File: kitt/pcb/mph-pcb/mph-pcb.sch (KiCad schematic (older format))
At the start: 15 parts, among them U1 TLC5940NT, U2 TLC5940NT, U3 TLC5940NT, U4 TLC5940NT, U5 TLC5940NT, U6 TLC5940NT, U7 TLC5940NT

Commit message: first four 7-segment displays
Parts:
- added DISP1, DISP2, DISP3, DISP4: LDS-A816RI, Display_7Segment:7SegmentLED_LDSA816RI_LDSA816RI, symbol Display_Character:LDS-A816RI
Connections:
- net labels added: DISP1_A, DISP1_B, DISP1_C, DISP1_D, DISP1_E, DISP1_F, DISP1_G, DISP1_RDP, DISP2_A, DISP2_B, DISP2_C, DISP2_D, DISP2_E, DISP2_F, DISP2_G, DISP2_RDP, DISP3_A, DISP3_B, DISP3_C, DISP3_D, DISP3_E, DISP3_F, DISP3_G, DISP3_RDP, DISP4_A, DISP4_B, DISP4_C, DISP4_D, DISP4_E, DISP4_F, DISP4_G, DISP4_RDP
- wire segments 65 -> 117
- no-connect marks 14 -> 18

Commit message: store all libraries in project
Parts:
- DISP1, DISP2, DISP3, DISP4: symbol Display_Character:LDS-A816RI -> KITT-Symbols:LDS-A816RI
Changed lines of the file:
@@
 NoConn ~ 3450 14600
 $Comp
-L Display_Character:LDS-A816RI DISP1
+L KITT-Symbols:LDS-A816RI DISP1
 U 1 1 61139383
 P 3500 9100
@@
 NoConn ~ 4000 9400
 $Comp
-L Display_Character:LDS-A816RI DISP2
+L KITT-Symbols:LDS-A816RI DISP2
 U 1 1 6114598A
 P 5000 9100
@@
 NoConn ~ 5500 9400
 $Comp
-L Display_Character:LDS-A816RI DISP3
+L KITT-Symbols:LDS-A816RI DISP3
 U 1 1 61149F6E
 P 6500 9100
@@
 NoConn ~ 7000 9400
 $Comp
-L Display_Character:LDS-A816RI DISP4
+L KITT-Symbols:LDS-A816RI DISP4
 U 1 1 6114DA45
 P 8000 9100

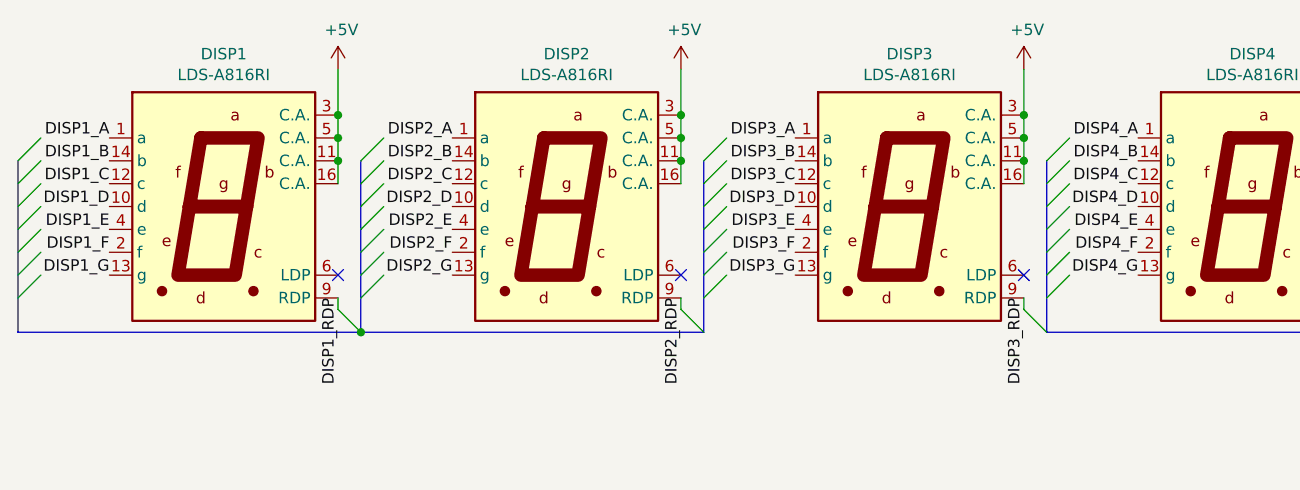
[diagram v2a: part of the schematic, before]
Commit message: wire up a-f on displays
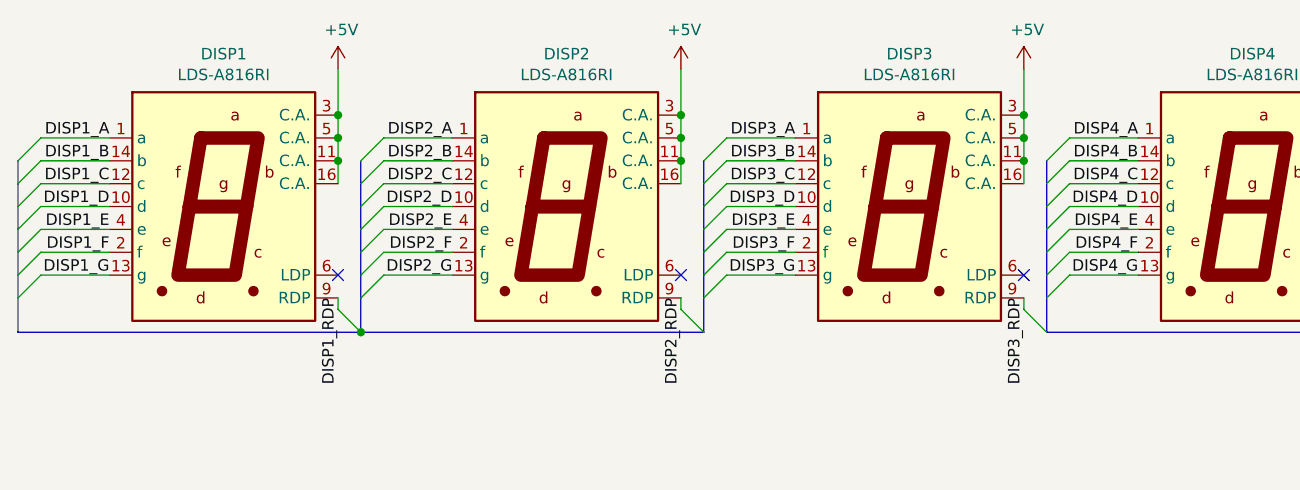
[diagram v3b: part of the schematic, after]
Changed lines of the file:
@@
 Wire Wire Line
 	7400 10500 7400 10950
+Wire Wire Line
+	2700 8800 3000 8800
+Wire Wire Line
+	2700 8900 3000 8900
+Wire Wire Line
+	2700 9000 3000 9000
+Wire Wire Line
+	3000 9100 2700 9100
+Wire Wire Line
+	3000 9200 2700 9200
+Wire Wire Line
+	3000 9300 2700 9300
+Wire Wire Line
+	3000 9400 2700 9400
+Wire Wire Line
+	4500 9400 4200 9400
+Wire Wire Line
+	4500 9300 4200 9300
+Wire Wire Line
+	4500 9200 4200 9200
+Wire Wire Line
+	4500 9100 4200 9100
+Wire Wire Line
+	4500 9000 4200 9000
+Wire Wire Line
+	4500 8900 4200 8900
+Wire Wire Line
+	4500 8800 4200 8800
+Wire Wire Line
+	6000 9400 5700 9400
+Wire Wire Line
+	6000 9300 5700 9300
+Wire Wire Line
+	6000 9200 5700 9200
+Wire Wire Line
+	6000 9100 5700 9100
+Wire Wire Line
+	6000 9000 5700 9000
+Wire Wire Line
+	6000 8900 5700 8900
+Wire Wire Line
+	6000 8800 5700 8800
+Wire Wire Line
+	7500 9400 7200 9400
+Wire Wire Line
+	7500 9300 7200 9300
+Wire Wire Line
+	7500 9200 7200 9200
+Wire Wire Line
+	7500 9100 7200 9100
+Wire Wire Line
+	7500 9000 7200 9000
+Wire Wire Line
+	7500 8900 7200 8900
+Wire Wire Line
+	7500 8800 7200 8800
 Wire Bus Line
 	2900 13250 2900 14700

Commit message: fixed footpads
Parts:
- DISP1, DISP2, DISP3, DISP4: footprint Display_7Segment:7SegmentLED_LDSA816RI_LDSA816RI -> KITT-Footpads:LDS-A816RI
- TTGO1: footprint TTGO-tdisplay:TTGO_ESP32_TDisplay_v1.1 -> KITT-Footpads:TTGO_ESP32_TDisplay_v1.1
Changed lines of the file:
@@
 F 0 "TTGO1" H 4000 16587 60  0000 C CNN
 F 1 "TTGO_ESP32_TDISPLAY_V1.1" H 4000 16481 60  0000 C CNN
-F 2 "TTGO-tdisplay:TTGO_ESP32_TDisplay_v1.1" H 3650 15150 60  0001 C CNN
+F 2 "KITT-Footpads:TTGO_ESP32_TDisplay_v1.1" H 3650 15150 60  0001 C CNN
 F 3 "" H 3650 15150 60  0001 C CNN
 	1    3650 15150
@@
 F 0 "DISP1" H 3500 9767 50  0000 C CNN
 F 1 "LDS-A816RI" H 3500 9676 50  0000 C CNN
-F 2 "Display_7Segment:7SegmentLED_LDSA816RI_LDSA816RI" H 3500 8500 50  0001 C CNN
-F 3 "https://datasheet.octopart.com/LTS-6960HR-Lite-On-datasheet-11803242.pdf" H 4450 9050 50  0001 C CNN
+F 2 "KITT-Footpads:LDS-A816RI" H 3500 8500 50  0001 C CNN
+F 3 "https://www.lumex.com/datasheet/LDS-A816RI" H 4450 9050 50  0001 C CNN
 	1    3500 9100
 	1    0    0    -1
@@
 	4000 8900 4000 8800
 $Comp
-L power:+5V #PWR?
+L power:+5V #PWR0128
 U 1 1 6113BF63
 P 4000 8500
-F 0 "#PWR?" H 4000 8350 50  0001 C CNN
+F 0 "#PWR0128" H 4000 8350 50  0001 C CNN
 F 1 "+5V" H 4015 8673 50  0000 C CNN
 F 2 "" H 4000 8500 50  0001 C CNN
@@
 F 0 "DISP2" H 5000 9767 50  0000 C CNN
 F 1 "LDS-A816RI" H 5000 9676 50  0000 C CNN
-F 2 "Display_7Segment:7SegmentLED_LDSA816RI_LDSA816RI" H 5000 8500 50  0001 C CNN
-F 3 "https://datasheet.octopart.com/LTS-6960HR-Lite-On-datasheet-11803242.pdf" H 5950 9050 50  0001 C CNN
+F 2 "KITT-Footpads:LDS-A816RI" H 5000 8500 50  0001 C CNN
+F 3 "https://www.lumex.com/datasheet/LDS-A816RI" H 5950 9050 50  0001 C CNN
 	1    5000 9100
 	1    0    0    -1
@@
 	5500 8900 5500 8800
 $Comp
-L power:+5V #PWR?
+L power:+5V #PWR0129
 U 1 1 61145997
 P 5500 8500
-F 0 "#PWR?" H 5500 8350 50  0001 C CNN
+F 0 "#PWR0129" H 5500 8350 50  0001 C CNN
 F 1 "+5V" H 5515 8673 50  0000 C CNN
 F 2 "" H 5500 8500 50  0001 C CNN
@@
 F 0 "DISP3" H 6500 9767 50  0000 C CNN
 F 1 "LDS-A816RI" H 6500 9676 50  0000 C CNN
-F 2 "Display_7Segment:7SegmentLED_LDSA816RI_LDSA816RI" H 6500 8500 50  0001 C CNN
-F 3 "https://datasheet.octopart.com/LTS-6960HR-Lite-On-datasheet-11803242.pdf" H 7450 9050 50  0001 C CNN
+F 2 "KITT-Footpads:LDS-A816RI" H 6500 8500 50  0001 C CNN
+F 3 "https://www.lumex.com/datasheet/LDS-A816RI" H 7450 9050 50  0001 C CNN
 	1    6500 9100
 	1    0    0    -1
@@
 	7000 8900 7000 8800
 $Comp
-L power:+5V #PWR?
+L power:+5V #PWR0130
 U 1 1 61149F7B
 P 7000 8500
-F 0 "#PWR?" H 7000 8350 50  0001 C CNN
+F 0 "#PWR0130" H 7000 8350 50  0001 C CNN
 F 1 "+5V" H 7015 8673 50  0000 C CNN
 F 2 "" H 7000 8500 50  0001 C CNN
@@
 F 0 "DISP4" H 8000 9767 50  0000 C CNN
 F 1 "LDS-A816RI" H 8000 9676 50  0000 C CNN
-F 2 "Display_7Segment:7SegmentLED_LDSA816RI_LDSA816RI" H 8000 8500 50  0001 C CNN
-F 3 "https://datasheet.octopart.com/LTS-6960HR-Lite-On-datasheet-11803242.pdf" H 8950 9050 50  0001 C CNN
+F 2 "KITT-Footpads:LDS-A816RI" H 8000 8500 50  0001 C CNN
+F 3 "https://www.lumex.com/datasheet/LDS-A816RI" H 8950 9050 50  0001 C CNN
 	1    8000 9100
 	1    0    0    -1
@@
 	8500 8900 8500 8800
 $Comp
-L power:+5V #PWR?
+L power:+5V #PWR0131
 U 1 1 6114DA52
 P 8500 8500
-F 0 "#PWR?" H 8500 8350 50  0001 C CNN
+F 0 "#PWR0131" H 8500 8350 50  0001 C CNN
 F 1 "+5V" H 8515 8673 50  0000 C CNN
 F 2 "" H 8500 8500 50  0001 C CNN

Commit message: add coupling capacitors
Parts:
- added C1: 100nF, symbol Device:C
- added C2: 1uF, symbol Device:C
- added C3, C4, C5, C6, C7, C8, C9: 100nF, Capacitor_THT:C_Rect_L7.0mm_W3.5mm_P5.00mm, symbol Device:C
- R1, R2, R3, R4, R5, R7: footprint (none) -> Resistor_THT:R_Axial_DIN0207_L6.3mm_D2.5mm_P10.16mm_Horizontal
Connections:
- net +5V: now also C1.1, C2.1, C3.1, C4.1, C5.1, C6.1, C7.1, C8.1, C9.1
- net GND: now also C1.2, C2.2, C3.2, C4.2, C5.2, C6.2, C7.2, C8.2, C9.2

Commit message: fixed missing footpads
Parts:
- C1, C2: footprint (none) -> Capacitor_THT:C_Rect_L7.0mm_W3.5mm_P5.00mm
- R6: footprint (none) -> Resistor_THT:R_Axial_DIN0207_L6.3mm_D2.5mm_P10.16mm_Horizontal
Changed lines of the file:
@@
 F 0 "R6" H 16470 12796 50  0000 L CNN
 F 1 "2.2K" H 16470 12705 50  0000 L CNN
-F 2 "" V 16330 12750 50  0001 C CNN
+F 2 "Resistor_THT:R_Axial_DIN0207_L6.3mm_D2.5mm_P10.16mm_Horizontal" V 16330 12750 50  0001 C CNN
 F 3 "~" H 16400 12750 50  0001 C CNN
 	1    16400 12750
@@
 $EndComp
 $Comp
-L power:GND #PWR?
+L power:GND #PWR0132
 U 1 1 61134539
 P 2800 11950
-F 0 "#PWR?" H 2800 11700 50  0001 C CNN
+F 0 "#PWR0132" H 2800 11700 50  0001 C CNN
 F 1 "GND" H 2805 11777 50  0000 C CNN
 F 2 "" H 2800 11950 50  0001 C CNN
@@
 $EndComp
 $Comp
-L power:GND #PWR?
+L power:GND #PWR0133
 U 1 1 6115CD6C
 P 5400 11950
-F 0 "#PWR?" H 5400 11700 50  0001 C CNN
+F 0 "#PWR0133" H 5400 11700 50  0001 C CNN
 F 1 "GND" H 5405 11777 50  0000 C CNN
 F 2 "" H 5400 11950 50  0001 C CNN
@@
 $EndComp
 $Comp
-L power:GND #PWR?
+L power:GND #PWR0134
 U 1 1 6116FAF1
 P 8000 11950
-F 0 "#PWR?" H 8000 11700 50  0001 C CNN
+F 0 "#PWR0134" H 8000 11700 50  0001 C CNN
 F 1 "GND" H 8005 11777 50  0000 C CNN
 F 2 "" H 8000 11950 50  0001 C CNN
@@
 $EndComp
 $Comp
-L power:GND #PWR?
+L power:GND #PWR0135
 U 1 1 61182311
 P 10600 11950
-F 0 "#PWR?" H 10600 11700 50  0001 C CNN
+F 0 "#PWR0135" H 10600 11700 50  0001 C CNN
 F 1 "GND" H 10605 11777 50  0000 C CNN
 F 2 "" H 10600 11950 50  0001 C CNN
@@
 $EndComp
 $Comp
-L power:GND #PWR?
+L power:GND #PWR0136
 U 1 1 611950CA
 P 13200 11950
-F 0 "#PWR?" H 13200 11700 50  0001 C CNN
+F 0 "#PWR0136" H 13200 11700 50  0001 C CNN
 F 1 "GND" H 13205 11777 50  0000 C CNN
 F 2 "" H 13200 11950 50  0001 C CNN
@@
 $EndComp
 $Comp
-L power:GND #PWR?
+L power:GND #PWR0137
 U 1 1 611A7D7F
 P 15800 11950
-F 0 "#PWR?" H 15800 11700 50  0001 C CNN
+F 0 "#PWR0137" H 15800 11700 50  0001 C CNN
 F 1 "GND" H 15805 11777 50  0000 C CNN
 F 2 "" H 15800 11950 50  0001 C CNN
@@
 $EndComp
 $Comp
-L power:GND #PWR?
+L power:GND #PWR0138
 U 1 1 611BAA79
 P 18400 11950
-F 0 "#PWR?" H 18400 11700 50  0001 C CNN
+F 0 "#PWR0138" H 18400 11700 50  0001 C CNN
 F 1 "GND" H 18405 11777 50  0000 C CNN
 F 2 "" H 18400 11950 50  0001 C CNN
@@
 F 0 "C1" H 4665 15296 50  0000 L CNN
 F 1 "100nF" H 4665 15205 50  0000 L CNN
-F 2 "" H 4588 15100 50  0001 C CNN
+F 2 "Capacitor_THT:C_Rect_L7.0mm_W3.5mm_P5.00mm" H 4588 15100 50  0001 C CNN
 F 3 "~" H 4550 15250 50  0001 C CNN
 	1    4550 15250
@@
 Connection ~ 4550 15100
 $Comp
-L power:GND #PWR?
+L power:GND #PWR0139
 U 1 1 611E2E2D
 P 4550 15400
-F 0 "#PWR?" H 4550 15150 50  0001 C CNN
+F 0 "#PWR0139" H 4550 15150 50  0001 C CNN
 F 1 "GND" H 4555 15227 50  0000 C CNN
 F 2 "" H 4550 15400 50  0001 C CNN
@@
 F 0 "C2" H 5165 15296 50  0000 L CNN
 F 1 "1uF" H 5165 15205 50  0000 L CNN
-F 2 "" H 5088 15100 50  0001 C CNN
+F 2 "Capacitor_THT:C_Rect_L7.0mm_W3.5mm_P5.00mm" H 5088 15100 50  0001 C CNN
 F 3 "~" H 5050 15250 50  0001 C CNN
 	1    5050 15250
@@
 Connection ~ 5050 15100
 $Comp
-L power:GND #PWR?
+L power:GND #PWR0140
 U 1 1 611191EF
 P 5050 15400
-F 0 "#PWR?" H 5050 15150 50  0001 C CNN
+F 0 "#PWR0140" H 5050 15150 50  0001 C CNN
 F 1 "GND" H 5055 15227 50  0000 C CNN
 F 2 "" H 5050 15400 50  0001 C CNN

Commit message: finished wiring
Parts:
- added D25, D26, D27, HT1, HT10, HT11, HT12, HT13, HT14, HT15, HT16, HT2, HT3, HT4, HT5, HT6, HT7, HT8, HT9, HY1, HY2, HY3, MY1, MY2, MY3, UG1, UG10, UG11, UG12, UG13, UG14, UG15, UG16, UG17, UG18, UG19, UG2, UG20, UG3, UG4, UG5, UG6, UG7, UG8, UG9, UGY1, UGY2, UGY3: LED, symbol Device:LED
- added GUID1, GUID2, SYST1, SYST2: DF3GD, symbol KITT-Symbols:DF3GD
- added J1, J2: Screw_Terminal_01x02, symbol Connector:Screw_Terminal_01x02
- added LVL1: LVL_5V_3V3, symbol KITT-Symbols:LVL_5V_3V3
- added PWR1: OKI-78SR-3.3_1.5-W36H-C, Converter_DCDC:Converter_DCDC_muRata_OKI-78SR_Horizontal, symbol Converter_DCDC:OKI-78SR-3.3_1.5-W36H-C
- added R10, R11, R12, R13, R14, R15, R16, R17, R18, R19, R8, R9: 120R, Resistor_THT:R_Axial_DIN0207_L6.3mm_D2.5mm_P10.16mm_Horizontal, symbol Device:R
- added UT_DISP1, UT_DISP2, UT_DISP3: LDS-A816RI, KITT-Footpads:LDS-A816RI, symbol KITT-Symbols:LDS-A816RI
- renumbered DISP2 to HLT_DISP2, DISP1 to MASH_DISP1, DISP3 to MASH_DISP3, DISP4 to MASH_DISP4
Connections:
- net +5V: now also D25.2 (A), D26.2 (A), D27.2 (A), HT1.2 (A), HT10.2 (A), HT11.2 (A), HT12.2 (A), HT13.2 (A), HT14.2 (A), HT15.2 (A), HT16.2 (A), HT2.2 (A), HT3.2 (A), HT4.2 (A), HT5.2 (A), HT6.2 (A), HT7.2 (A), HT8.2 (A), HT9.2 (A), HY1.2 (A), HY2.2 (A), HY3.2 (A), LVL1.1 (5V), MY1.2 (A), MY2.2 (A), MY3.2 (A), PWR1.3 (OUT), R10.1, R11.1, R12.1, R13.1, R14.1, R15.1, R16.1, R17.1, R18.1, R19.1, R8.1, R9.1, UG1.2 (A), UG10.2 (A), UG11.2 (A), UG12.2 (A), UG13.2 (A), UG14.2 (A), UG15.2 (A), UG16.2 (A), UG17.2 (A), UG18.2 (A), UG19.2 (A), UG2.2 (A), UG20.2 (A), UG3.2 (A), UG4.2 (A), UG5.2 (A), UG6.2 (A), UG7.2 (A), UG8.2 (A), UG9.2 (A), UGY1.2 (A), UGY2.2 (A), UGY3.2 (A), UT_DISP1.11 (C.A.), UT_DISP1.16 (C.A.), UT_DISP1.3 (C.A.), UT_DISP1.5 (C.A.), UT_DISP2.11 (C.A.), UT_DISP2.16 (C.A.), UT_DISP2.3 (C.A.), UT_DISP2.5 (C.A.), UT_DISP3.11 (C.A.), UT_DISP3.16 (C.A.), UT_DISP3.3 (C.A.), UT_DISP3.5 (C.A.)
- net GND: now also GUID1.2 (D3C), GUID1.4 (D2C), GUID1.6 (D1C), GUID2.2 (D3C), GUID2.4 (D2C), GUID2.6 (D1C), J1.2 (Pin_2), LVL1.11 (GND), LVL1.2 (GND), PWR1.2 (GND), SYST1.2 (D3C), SYST1.4 (D2C), SYST1.6 (D1C), SYST2.2 (D3C), SYST2.4 (D2C), SYST2.6 (D1C)
- net LV_TX: now reaches TTGO1.15 (GPIO21)
- net LV_TX: now also LVL1.10 (LV1)
- net LV_RX: now reaches TTGO1.16 (GPIO22)
- net LV_RX: now also LVL1.9 (LV2)
- net at TTGO1.24 (3.3V): now also LVL1.12 (3V3)
- net HTL_D2: now reaches U3.1 (OUT1)
- net HTL_D2: now also HT2.1 (K)
- net HTL_D11: now reaches U3.10 (OUT10)
- net HTL_D11: now also HT11.1 (K)
- net HTL_D12: now reaches U3.11 (OUT11)
- net HTL_D12: now also HT12.1 (K)
- net HTL_D13: now reaches U3.12 (OUT12)
- net HTL_D13: now also HT13.1 (K)
- net HTL_D14: now reaches U3.13 (OUT13)
- net HTL_D14: now also HT14.1 (K)
- net HTL_D15: now reaches U3.14 (OUT14)
- net HTL_D15: now also HT15.1 (K)
- net HTL_D16: now reaches U3.15 (OUT15)
- net HTL_D16: now also HT16.1 (K)
- net HTL_D3: now reaches U3.2 (OUT2)
- net HTL_D3: now also HT3.1 (K)
- net HTL_D1: now reaches U3.28 (OUT0)
- net HTL_D1: now also HT1.1 (K)
- net HTL_D4: now reaches U3.3 (OUT3)
- net HTL_D4: now also HT4.1 (K)
- net HTL_D5: now reaches U3.4 (OUT4)
- net HTL_D5: now also HT5.1 (K)
- net HTL_D6: now reaches U3.5 (OUT5)
- net HTL_D6: now also HT6.1 (K)
- net HTL_D7: now reaches U3.6 (OUT6)
- net HTL_D7: now also HT7.1 (K)
- net HTL_D8: now reaches U3.7 (OUT7)
- net HTL_D8: now also HT8.1 (K)
- net HTL_D9: now reaches U3.8 (OUT8)
- net HTL_D9: now also HT9.1 (K)
- net HTL_D10: now reaches U3.9 (OUT9)
- net HTL_D10: now also HT10.1 (K)
- net MASH_YD2: now reaches U4.1 (OUT1)
- net MASH_YD2: now also MY2.1 (K)
- net UT_YD2: now reaches U4.10 (OUT10)
- net UT_YD2: now also D26.1 (K)
- net UT_YD3: now reaches U4.11 (OUT11)
- net UT_YD3: now also D27.1 (K)
- net UG_D1: now reaches U4.12 (OUT12)
- net UG_D1: now also UG1.1 (K)
- net UG_D2: now reaches U4.13 (OUT13)
- net UG_D2: now also UG2.1 (K)
- net UG_D3: now reaches U4.14 (OUT14)
- net UG_D3: now also UG3.1 (K)
- net UG_D4: now reaches U4.15 (OUT15)
- net UG_D4: now also UG4.1 (K)
- net MASH_YD3: now reaches U4.2 (OUT2)
- net MASH_YD3: now also MY3.1 (K)
- net MASH_YD1: now reaches U4.28 (OUT0)
- net MASH_YD1: now also MY1.1 (K)
- net HLT_YD1: now reaches U4.3 (OUT3)
- net HLT_YD1: now also HY1.1 (K)
- net HLT_YD2: now reaches U4.4 (OUT4)
- net HLT_YD2: now also HY2.1 (K)
- net HLT_YD3: now reaches U4.5 (OUT5)
- net HLT_YD3: now also HY3.1 (K)
- net UG_YD1: now reaches U4.6 (OUT6)
- net UG_YD1: now also UGY1.1 (K)
- net UG_YD2: now reaches U4.7 (OUT7)
- net UG_YD2: now also UGY2.1 (K)
- net UG_YD3: now reaches U4.8 (OUT8)
- net UG_YD3: now also UGY3.1 (K)
- net UT_YD1: now reaches U4.9 (OUT9)
- net UT_YD1: now also D25.1 (K)
- net UG_D6: now reaches U5.1 (OUT1)
- net UG_D6: now also UG6.1 (K)
- net UG_D15: now reaches U5.10 (OUT10)
- net UG_D15: now also UG15.1 (K)
- net UG_D16: now reaches U5.11 (OUT11)
- net UG_D16: now also UG16.1 (K)
- net UG_D17: now reaches U5.12 (OUT12)
- net UG_D17: now also UG17.1 (K)
- net UG_D18: now reaches U5.13 (OUT13)
- net UG_D18: now also UG18.1 (K)
- net UG_D19: now reaches U5.14 (OUT14)
- net UG_D19: now also UG19.1 (K)
- net UG_D20: now reaches U5.15 (OUT15)
- net UG_D20: now also UG20.1 (K)
- net UG_D7: now reaches U5.2 (OUT2)
- net UG_D7: now also UG7.1 (K)
- net UG_D5: now reaches U5.28 (OUT0)
- net UG_D5: now also UG5.1 (K)
- net UG_D8: now reaches U5.3 (OUT3)
- net UG_D8: now also UG8.1 (K)
- net UG_D9: now reaches U5.4 (OUT4)
- net UG_D9: now also UG9.1 (K)
- net UG_D10: now reaches U5.5 (OUT5)
- net UG_D10: now also UG10.1 (K)
- net UG_D11: now reaches U5.6 (OUT6)
- net UG_D11: now also UG11.1 (K)
- net UG_D12: now reaches U5.7 (OUT7)
- net UG_D12: now also UG12.1 (K)
- net UG_D13: now reaches U5.8 (OUT8)
- net UG_D13: now also UG13.1 (K)
- net UG_D14: now reaches U5.9 (OUT9)
- net UG_D14: now also UG14.1 (K)
- net UT_DISP1_F: now reaches U6.1 (OUT1)
- net UT_DISP1_F: now also UT_DISP1.2 (f)
- net UT_DISP2_E: now reaches U6.10 (OUT10)
- net UT_DISP2_E: now also UT_DISP2.4 (e)
- net UT_DISP2_RDP: now reaches U6.11 (OUT11)
- net UT_DISP2_RDP: now also UT_DISP2.9 (RDP)
- net UT_DISP2_D: now reaches U6.12 (OUT12)
- net UT_DISP2_D: now also UT_DISP2.10 (d)
- net UT_DISP2_C: now reaches U6.13 (OUT13)
- net UT_DISP2_C: now also UT_DISP2.12 (c)
- net UT_DISP2_G: now reaches U6.14 (OUT14)
- net UT_DISP2_G: now also UT_DISP2.13 (g)
- net UT_DISP2_B: now reaches U6.15 (OUT15)
- net UT_DISP2_B: now also UT_DISP2.14 (b)
- net UT_DISP1_E: now reaches U6.2 (OUT2)
- net UT_DISP1_E: now also UT_DISP1.4 (e)
- net UT_DISP1_A: now reaches U6.28 (OUT0)
- net UT_DISP1_A: now also UT_DISP1.1 (a)
- net UT_DISP1_RDP: now reaches U6.3 (OUT3)
- net UT_DISP1_RDP: now also UT_DISP1.9 (RDP)
- net UT_DISP1_D: now reaches U6.4 (OUT4)
- net UT_DISP1_D: now also UT_DISP1.10 (d)
- net UT_DISP1_C: now reaches U6.5 (OUT5)
- net UT_DISP1_C: now also UT_DISP1.12 (c)
- net UT_DISP1_G: now reaches U6.6 (OUT6)
- net UT_DISP1_G: now also UT_DISP1.13 (g)
- net UT_DISP1_B: now reaches U6.7 (OUT7)
- net UT_DISP1_B: now also UT_DISP1.14 (b)
- net UT_DISP2_A: now reaches U6.8 (OUT8)
- net UT_DISP2_A: now also UT_DISP2.1 (a)
- net UT_DISP2_F: now reaches U6.9 (OUT9)
- net UT_DISP2_F: now also UT_DISP2.2 (f)
- net UT_DISP3_F: now reaches U7.1 (OUT1)
- net UT_DISP3_F: now also UT_DISP3.2 (f)
- net UT_DISP3_E: now reaches U7.2 (OUT2)
- net UT_DISP3_E: now also UT_DISP3.4 (e)
- net UT_DISP3_A: now reaches U7.28 (OUT0)
- net UT_DISP3_A: now also UT_DISP3.1 (a)
- net UT_DISP3_RDP: now reaches U7.3 (OUT3)
- net UT_DISP3_RDP: now also UT_DISP3.9 (RDP)
- net UT_DISP3_D: now reaches U7.4 (OUT4)
- net UT_DISP3_D: now also UT_DISP3.10 (d)
- net UT_DISP3_C: now reaches U7.5 (OUT5)
- net UT_DISP3_C: now also UT_DISP3.12 (c)
- net UT_DISP3_G: now reaches U7.6 (OUT6)
- net UT_DISP3_G: now also UT_DISP3.13 (g)
- net UT_DISP3_B: now reaches U7.7 (OUT7)
- net UT_DISP3_B: now also UT_DISP3.14 (b)
- net DISP1_A renamed MASH_DISP1_A
- net DISP1_B renamed MASH_DISP1_B
- net DISP1_C renamed MASH_DISP1_C
- net DISP1_D renamed MASH_DISP1_D
- net DISP1_E renamed MASH_DISP1_E
- net DISP1_F renamed MASH_DISP1_F
- net DISP1_G renamed MASH_DISP1_G
- net DISP1_RDP renamed MASH_DISP1_RDP
- net DISP2_A renamed MASH_DISP2_A
- net DISP2_B renamed MASH_DISP2_B
- net DISP2_C renamed MASH_DISP2_C
- net DISP2_D renamed MASH_DISP2_D
- net DISP2_E renamed MASH_DISP2_E
- net DISP2_F renamed MASH_DISP2_F
- net DISP2_G renamed MASH_DISP2_G
- net DISP2_RDP renamed MASH_DISP2_RDP
- net DISP3_A renamed MASH_DISP3_A
- net DISP3_B renamed MASH_DISP3_B
- net DISP3_C renamed MASH_DISP3_C
- net DISP3_D renamed MASH_DISP3_D
- net DISP3_E renamed MASH_DISP3_E
- net DISP3_F renamed MASH_DISP3_F
- net DISP3_G renamed MASH_DISP3_G
- net DISP3_RDP renamed MASH_DISP3_RDP
- net DISP4_A renamed MASH_DISP4_A
- net DISP4_B renamed MASH_DISP4_B
- net DISP4_C renamed MASH_DISP4_C
- net DISP4_D renamed MASH_DISP4_D
- net DISP4_E renamed MASH_DISP4_E
- net DISP4_F renamed MASH_DISP4_F
- net DISP4_G renamed MASH_DISP4_G
- net DISP4_RDP renamed MASH_DISP4_RDP
- new net: GUID1.1 (D3A), R16.2
- new net: GUID1.3 (D2A), R15.2
- new net: GUID1.5 (D1A), R14.2
- new net: GUID2.1 (D3A), R19.2
- new net: GUID2.3 (D2A), R18.2
- new net: GUID2.5 (D1A), R17.2
- new net: R10.2, SYST1.1 (D3A)
- new net: R9.2, SYST1.3 (D2A)
- new net: R8.2, SYST1.5 (D1A)
- new net: R13.2, SYST2.1 (D3A)
- new net: R12.2, SYST2.3 (D2A)
- new net: R11.2, SYST2.5 (D1A)
- new net: J1.1 (Pin_1), PWR1.1 (IN)
- new net HV_RX: J2.2 (Pin_2), LVL1.4 (HV2)
- new net HV_TX: J2.1 (Pin_1), LVL1.3 (HV1)
- no-connect marks 18 -> 32
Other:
- moved on the sheet: C1, C2, C3, C4, C5, C6, C7, C8, C9, HLT_DISP2, MASH_DISP1, MASH_DISP3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
